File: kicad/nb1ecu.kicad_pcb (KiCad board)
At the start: 4 copper layers, 154 x 159 mm, 108 parts, among them J1 Conn_01x01, J1 Conn_02x03_Top_Bottom, J2 Conn_01x01, J3 Conn_01x01, J4 Conn_01x01, J5 Conn_01x01, J6 Conn_01x01, P2 178780-1, Q1 PN2907A, Q10 DMG2302U, Q11 DMG2302U, Q12 DMG2302U, Q13 DMG2302U, Q14 DMG2302U, Q15 DMG2302U, Q16 DMG2302U, Q17 DMG2302U, Q2 PN2907A, Q3 DMG2302U, Q4 DMG2302U, Q5 DMG2302U, Q6 DMG2305UX, Q8 DMG2302U, Q9 DMG2302U, U1 Teensy4.1, U13 LMV324LIDT, U2 TL431LP, U3 MPX4250, U4 TC4424AVOA, U5 AP63205WU, U6 TC4424AVOA, U8 MPXHZ6115A

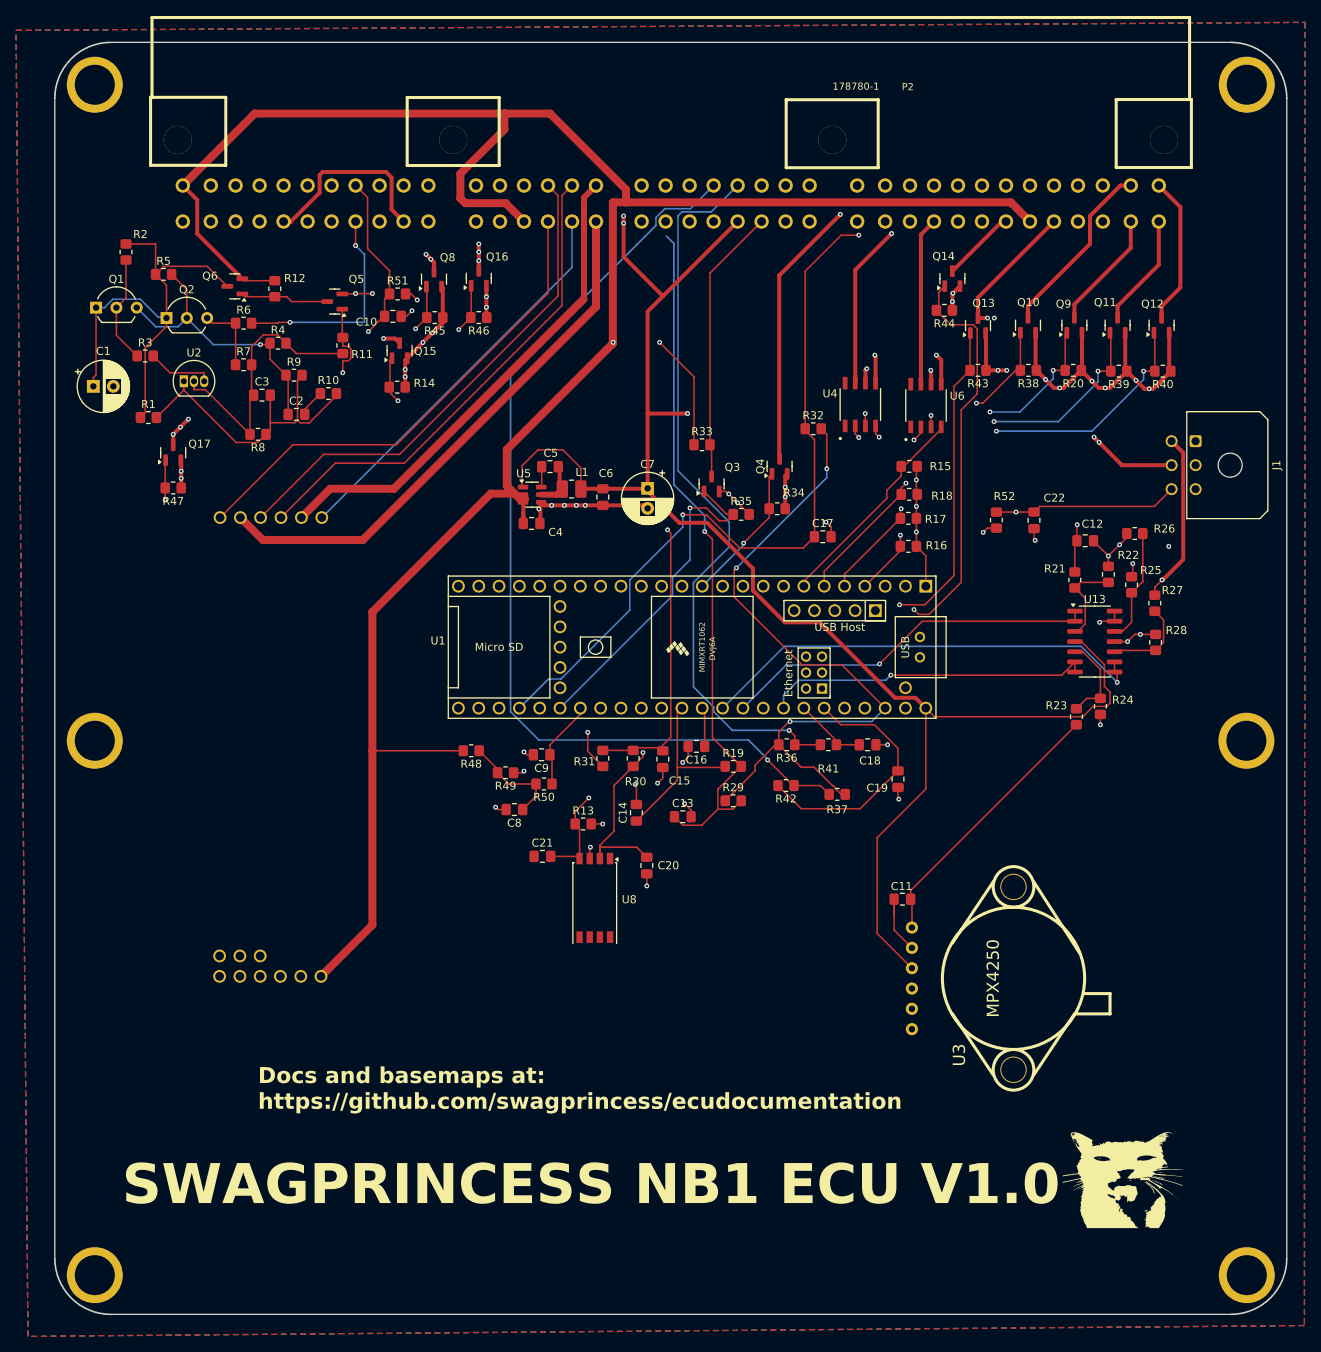
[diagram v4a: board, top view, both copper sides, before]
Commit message: add CANBUS
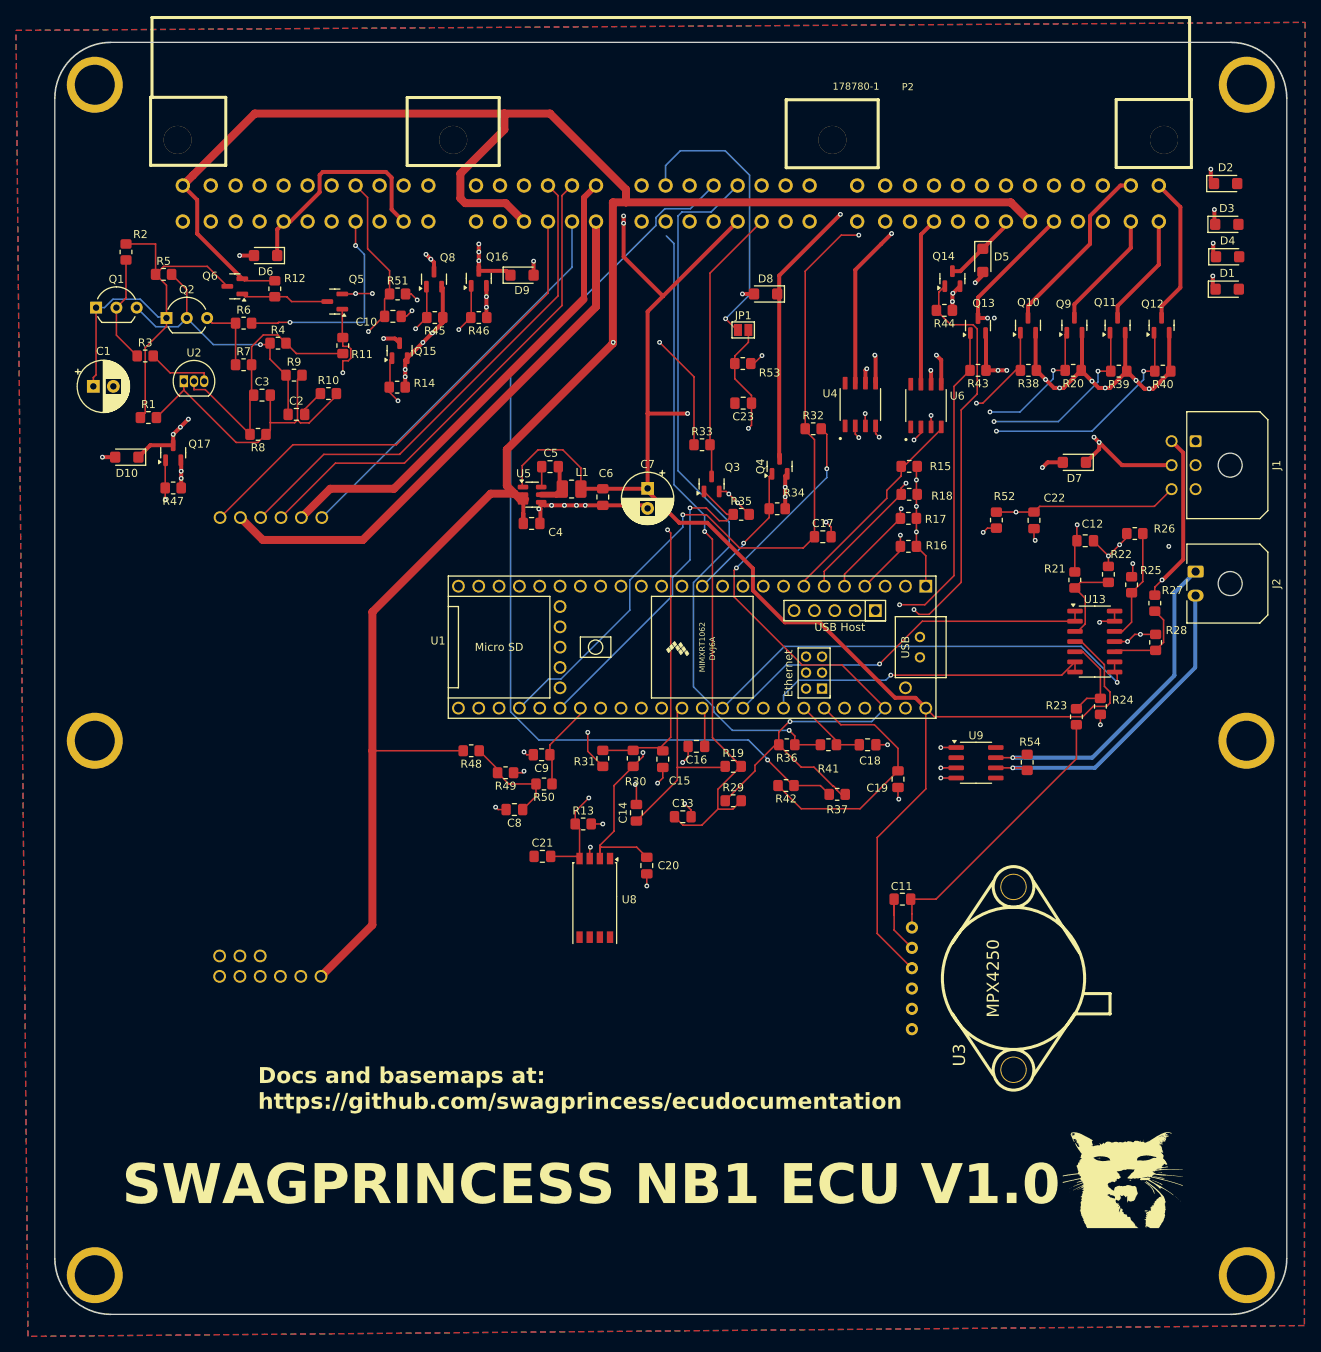
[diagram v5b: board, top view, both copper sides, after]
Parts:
- added C23: 220n, Capacitor_SMD:C_0805_2012Metric_Pad1.18x1.45mm_HandSolder, F.Cu at (104.7, 64.1)
- added D1: SMF15A, Diode_SMD:D_SMF, F.Cu at (165.2, 49.9)
- added D10: SMF15A, Diode_SMD:D_SMF, F.Cu at (27.6, 70.8)
- added D2: SMF15A, Diode_SMD:D_SMF, F.Cu at (164.9, 36.6)
- added D3: SMF15A, Diode_SMD:D_SMF, F.Cu at (165.1, 41.8)
- added D4: SMF15A, Diode_SMD:D_SMF, F.Cu at (165.2, 45.8)
- added D5: SMF15A, Diode_SMD:D_SMF, F.Cu at (134.6, 46.2)
- added D6: SMF15A, Diode_SMD:D_SMF, F.Cu at (45.0, 45.6)
- added D7: SMF15A, Diode_SMD:D_SMF, F.Cu at (146.1, 71.5)
- added D8: SMF15A, Diode_SMD:D_SMF, F.Cu at (107.5, 50.5)
- added D9: SMF15A, Diode_SMD:D_SMF, F.Cu at (77.0, 48.1)
- added J2: Conn_01x02, Connector_Molex:Molex_Micro-Fit_3.0_43650-0200_1x02_P3.00mm_Horizontal, F.Cu at (161.2, 85.2)
- added JP1: SolderJumper_2_Open, Jumper:SolderJumper-2_P1.3mm_Open_Pad1.0x1.5mm, F.Cu at (104.7, 55.0)
- added R53: 1k, Resistor_SMD:R_0805_2012Metric_Pad1.20x1.40mm_HandSolder, F.Cu at (104.6, 59.1)
- added R54: 120, Resistor_SMD:R_0805_2012Metric_Pad1.20x1.40mm_HandSolder, F.Cu at (140.2, 109.0)
- added U9: SN65HVD232, Package_SO:SOIC-8_3.9x4.9mm_P1.27mm, F.Cu at (133.8, 109.0)
- P2: footprint kicad:178780-1 -> conn-178780:178780-1
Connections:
- P2 pad 32: unconnected-(P2B-2D-Pad32) -> /VSS_IN
- U1 pad 33: unconnected-(U1-41_A17-Pad33) -> /VSS
- U1 pad 44: unconnected-(U1-22_A8_CTX1-Pad44) -> /CANTX
- U1 pad 45: unconnected-(U1-23_A9_CRX1_MCLK1-Pad45) -> /CANRX
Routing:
- net /VSS: track 0.00 -> 59.2 mm, vias 0 -> 1
- net /CANH: track 0.00 -> 42.6 mm, vias 0 -> 1
- net /CANL: track 0.00 -> 41.1 mm, vias 0 -> 1
- net /VSS_IN: track 0.00 -> 36.3 mm, vias 0 -> 1
- net +3V3: track 219.6 -> 251.2 mm, vias 6 -> 8
- net /CANTX: track 0.00 -> 16.0 mm, vias 0 -> 1
- net /CANRX: track 0.00 -> 15.0 mm, vias 0 -> 1
- net /INJ1_OUT: track 15.0 -> 29.8 mm, vias 0 -> 1
- net /INJ2_OUT: track 22.6 -> 35.4 mm, vias 0 -> 1
- net GND: track 207.8 -> 218.9 mm, vias 54 -> 60
- net /INJ4_OUT: track 18.6 -> 28.7 mm, vias 0 -> 1
- net /INJ3_OUT: track 14.2 -> 23.9 mm, vias 0 -> 1
- net /MAIN_FAN_OUT: track 48.0 -> 53.0 mm
- net /BOOST_OUT: track 20.7 -> 24.9 mm
- net /AC_FAN: track 33.9 -> 37.8 mm
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
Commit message: revision
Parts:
- added D11: 1N4448W, Diode_SMD:D_SOD-123, F.Cu at (104.1, 62.4)
- added R55: 10k, Resistor_SMD:R_0805_2012Metric_Pad1.20x1.40mm_HandSolder, F.Cu at (104.5, 69.2)
- D1, D10, D2, D3, D4, D5, D6, D7, D8, D9: value SMF15A -> 1N4448W; footprint Diode_SMD:D_SMF -> Diode_SMD:D_SOD-123
- moved D5 1.17 mm to (135.5, 45.5), turned to 180 degrees
- moved C23 1.00 mm to (104.7, 65.1)
- moved D9 0.63 mm to (76.7, 47.5), turned to 180 degrees
- moved D2 0.54 mm to (165.2, 37.1), turned to 180 degrees
- moved D3 0.22 mm to (165.3, 41.6), turned to 180 degrees
- moved D6 0.21 mm to (44.8, 45.6), turned to 0 degrees
- moved D1 0.16 mm to (165.2, 50.0), turned to 180 degrees
- moved D4 0.14 mm to (165.3, 45.9), turned to 180 degrees
- moved D10 0.10 mm to (27.5, 70.8), turned to 0 degrees
- moved D8 0.07 mm to (107.5, 50.4), turned to 0 degrees
- turned D7 to 0 degrees
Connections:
- D1 pad 1: /INJ1_OUT -> /12V_IGN
- D1 pad 2: GND -> /INJ1_OUT
- D10 pad 1: /MAIN_FAN_OUT -> /12V_IGN
- D10 pad 2: GND -> /MAIN_FAN_OUT
- D2 pad 1: /INJ2_OUT -> /12V_IGN
- D2 pad 2: GND -> /INJ2_OUT
- D3 pad 1: /INJ4_OUT -> /12V_IGN
- D3 pad 2: GND -> /INJ4_OUT
- D4 pad 1: /INJ3_OUT -> /12V_IGN
- D4 pad 2: GND -> /INJ3_OUT
- D5 pad 1: /IAC_OUT -> /12V_IGN
- D5 pad 2: GND -> /IAC_OUT
- D6 pad 1: /AC_FAN -> /12V_IGN
- D6 pad 2: GND -> /AC_FAN
- D7 pad 1: /VICS_OUT -> /12V_IGN
- D7 pad 2: GND -> /VICS_OUT
- D8 pad 1: /PUMP_OUT -> /12V_IGN
- D8 pad 2: GND -> /PUMP_OUT
- D9 pad 1: /BOOST_OUT -> /12V_IGN
- D9 pad 2: GND -> /BOOST_OUT
- JP1 pad 2: /VSS -> Net-(JP1-B)
- R53 pad 1: /VSS -> Net-(JP1-B)
- R53 pad 2: +3V3 -> /VSS
- U1 pad 10: /INJ3 -> /INJ4
- U1 pad 11: /INJ4 -> /INJ3
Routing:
- net /LAMBDA_5V: track 288.5 -> 181.5 mm
- net /IAT_SENS: track 134.9 -> 96.0 mm
- net +5V: track 315.8 -> 277.5 mm, vias 5 -> 3
- net +3V3: track 251.2 -> 280.6 mm, vias 8 -> 9
- net GND: track 218.9 -> 209.2 mm, vias 60 -> 55
- net Net-(JP1-B): track 0.00 -> 4.90 mm
- net /12V_IGN: track 352.6 -> 348.4 mm, vias 2 -> 11
- net /VSS: track 59.2 -> 55.5 mm
- net /INJ3: track 66.6 -> 69.1 mm, vias 2 -> 3
- net /INJ4: track 72.6 -> 70.0 mm
- net /INJ2_OUT: track 35.4 -> 36.5 mm
- net /BOOST_OUT: track 24.9 -> 24.2 mm
- net /VICS_OUT: vias 4 -> 3
- added copper zone on In2.Cu, net /12V_IGN
- removed copper zone on In2.Cu, net GND
